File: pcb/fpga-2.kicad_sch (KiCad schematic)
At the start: 3 parts

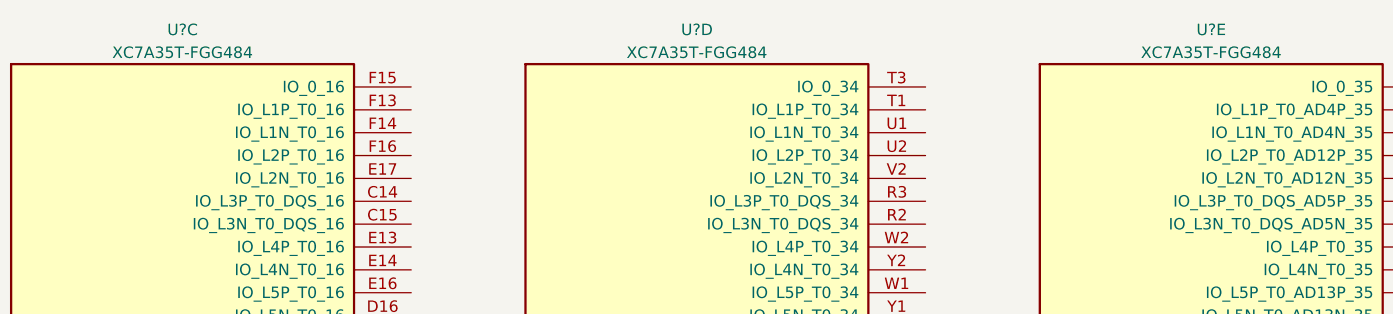
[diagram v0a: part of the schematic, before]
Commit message: addl. updates to power hierarchy
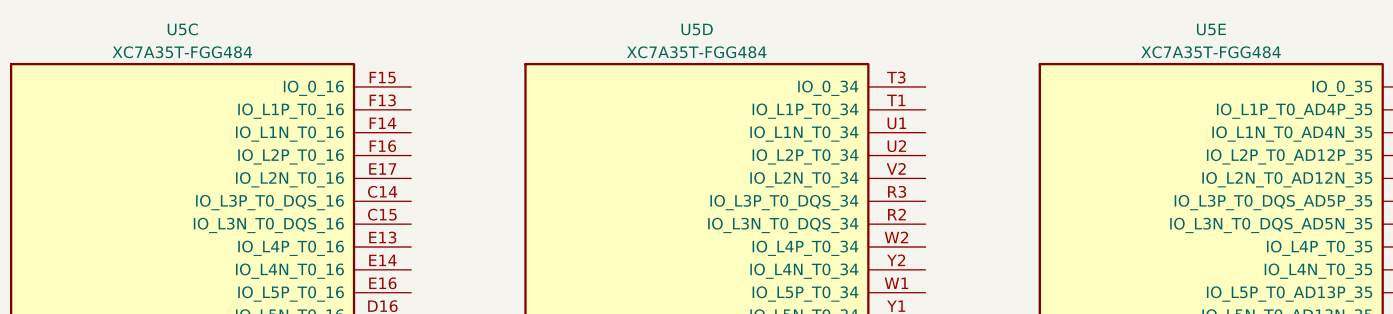
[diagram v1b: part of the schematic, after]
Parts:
- gave numbers to parts that had none: 1
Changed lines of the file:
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@@
 		(dnp no)
 		(fields_autoplaced yes)
-		(property "Reference" "U?"
+		(property "Reference" "U5"
 			(at 154.94 16.51 0)
 			(effects
@@
 			(project "RPi-HwAB-1"
 				(path "/e63e39d7-6ac0-4ffd-8aa3-1841a4541b55/6950ed9d-07bc-48b4-b7cb-d07910134e16"
-					(reference "U?")
+					(reference "U5")
 					(unit 5)
 				)
@@
 		(dnp no)
 		(fields_autoplaced yes)
-		(property "Reference" "U?"
+		(property "Reference" "U5"
 			(at 40.64 16.51 0)
 			(effects
@@
 			(project "RPi-HwAB-1"
 				(path "/e63e39d7-6ac0-4ffd-8aa3-1841a4541b55/6950ed9d-07bc-48b4-b7cb-d07910134e16"
-					(reference "U?")
+					(reference "U5")
 					(unit 3)
 				)
@@
 		(dnp no)
 		(fields_autoplaced yes)
-		(property "Reference" "U?"
+		(property "Reference" "U5"
 			(at 97.79 16.51 0)
 			(effects
@@
 			(project "RPi-HwAB-1"
 				(path "/e63e39d7-6ac0-4ffd-8aa3-1841a4541b55/6950ed9d-07bc-48b4-b7cb-d07910134e16"
-					(reference "U?")
+					(reference "U5")
 					(unit 4)
 				)

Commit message: added power sequencing through raspi gpio
additionally defined sensors
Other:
- company: (none) -> Andre S Winkel
- title: (none) -> RPi HwAB HAT+
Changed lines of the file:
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@@
 	(generator_version "9.0")
 	(paper "A4")
+	(title_block
+		(title "RPi HwAB HAT+")
+		(date "2025-08-23")
+		(rev "01")
+		(company "Andre S Winkel")
+	)
 	(symbol
 		(lib_id "FPGA_Xilinx_Artix7:XC7A35T-FGG484")

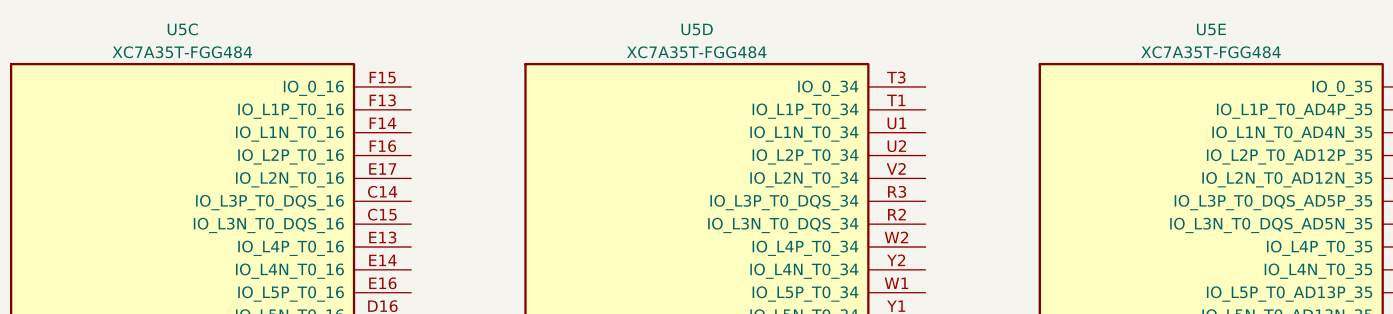
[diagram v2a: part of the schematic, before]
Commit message: reorg hierarchical, define buses
added bus definitions, aliasing, reorganized sub-sheets for hierarchical interpretation, grouped fpga. pending dram and mram addition
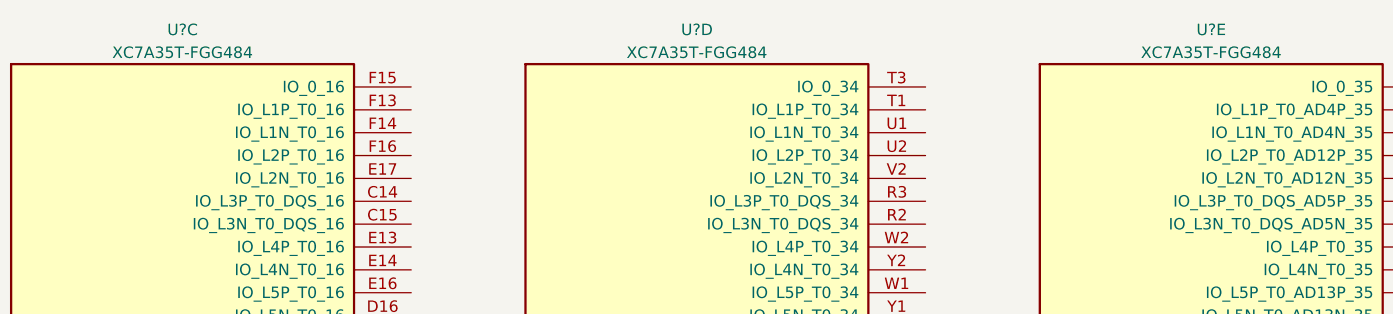
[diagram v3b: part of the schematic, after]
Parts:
- renumbered U5 to U?
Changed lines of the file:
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@@
 		(dnp no)
 		(fields_autoplaced yes)
-		(property "Reference" "U5"
+		(property "Reference" "U?"
 			(at 154.94 16.51 0)
 			(effects
@@
 		(instances
 			(project "RPi-HwAB-1"
-				(path "/e63e39d7-6ac0-4ffd-8aa3-1841a4541b55/6950ed9d-07bc-48b4-b7cb-d07910134e16"
-					(reference "U5")
+				(path "/e63e39d7-6ac0-4ffd-8aa3-1841a4541b55/59d21473-a004-4514-8090-fd93db818925/ef42fd34-c1d8-421f-b8cb-1078e483aec9"
+					(reference "U?")
 					(unit 5)
 				)
@@
 		(dnp no)
 		(fields_autoplaced yes)
-		(property "Reference" "U5"
+		(property "Reference" "U?"
 			(at 40.64 16.51 0)
 			(effects
@@
 		(instances
 			(project "RPi-HwAB-1"
-				(path "/e63e39d7-6ac0-4ffd-8aa3-1841a4541b55/6950ed9d-07bc-48b4-b7cb-d07910134e16"
-					(reference "U5")
+				(path "/e63e39d7-6ac0-4ffd-8aa3-1841a4541b55/59d21473-a004-4514-8090-fd93db818925/ef42fd34-c1d8-421f-b8cb-1078e483aec9"
+					(reference "U?")
 					(unit 3)
 				)
@@
 		(dnp no)
 		(fields_autoplaced yes)
-		(property "Reference" "U5"
+		(property "Reference" "U?"
 			(at 97.79 16.51 0)
 			(effects
@@
 		(instances
 			(project "RPi-HwAB-1"
-				(path "/e63e39d7-6ac0-4ffd-8aa3-1841a4541b55/6950ed9d-07bc-48b4-b7cb-d07910134e16"
-					(reference "U5")
+				(path "/e63e39d7-6ac0-4ffd-8aa3-1841a4541b55/59d21473-a004-4514-8090-fd93db818925/ef42fd34-c1d8-421f-b8cb-1078e483aec9"
+					(reference "U?")
 					(unit 4)
 				)

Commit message: completed bus aliasing definitions
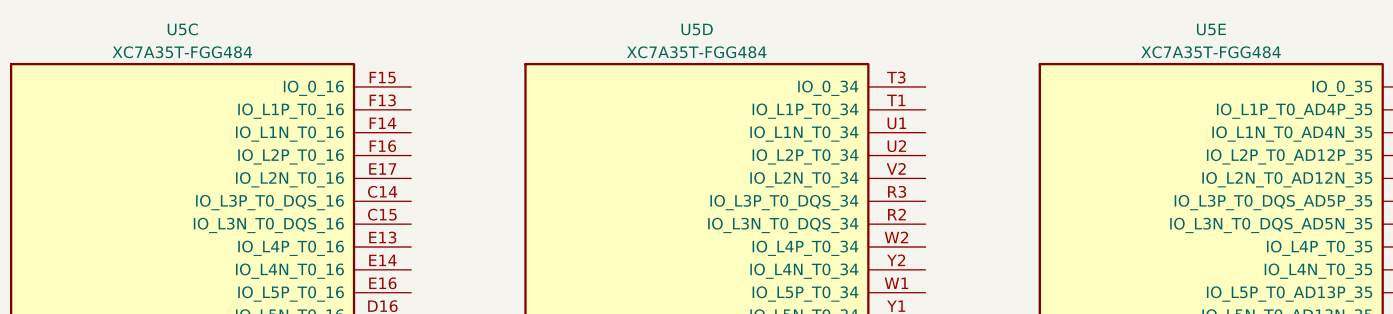
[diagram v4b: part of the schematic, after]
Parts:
- gave numbers to parts that had none: 1
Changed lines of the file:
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@@
 		(dnp no)
 		(fields_autoplaced yes)
-		(property "Reference" "U?"
+		(property "Reference" "U5"
 			(at 154.94 16.51 0)
 			(effects
@@
 			(project "RPi-HwAB-1"
 				(path "/e63e39d7-6ac0-4ffd-8aa3-1841a4541b55/59d21473-a004-4514-8090-fd93db818925/ef42fd34-c1d8-421f-b8cb-1078e483aec9"
-					(reference "U?")
+					(reference "U5")
 					(unit 5)
 				)
@@
 		(dnp no)
 		(fields_autoplaced yes)
-		(property "Reference" "U?"
+		(property "Reference" "U5"
 			(at 40.64 16.51 0)
 			(effects
@@
 			(project "RPi-HwAB-1"
 				(path "/e63e39d7-6ac0-4ffd-8aa3-1841a4541b55/59d21473-a004-4514-8090-fd93db818925/ef42fd34-c1d8-421f-b8cb-1078e483aec9"
-					(reference "U?")
+					(reference "U5")
 					(unit 3)
 				)
@@
 		(dnp no)
 		(fields_autoplaced yes)
-		(property "Reference" "U?"
+		(property "Reference" "U5"
 			(at 97.79 16.51 0)
 			(effects
@@
 			(project "RPi-HwAB-1"
 				(path "/e63e39d7-6ac0-4ffd-8aa3-1841a4541b55/59d21473-a004-4514-8090-fd93db818925/ef42fd34-c1d8-421f-b8cb-1078e483aec9"
-					(reference "U?")
+					(reference "U5")
 					(unit 4)
 				)

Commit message: saved libraries to project
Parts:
- U5: symbol FPGA_Xilinx_Artix7:XC7A35T-FGG484 -> library:XC7A35T-FGG484
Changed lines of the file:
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@@
 	)
 	(symbol
-		(lib_id "FPGA_Xilinx_Artix7:XC7A35T-FGG484")
+		(lib_id "library:XC7A35T-FGG484")
 		(at 154.94 85.09 0)
 		(unit 5)
@@
 	)
 	(symbol
-		(lib_id "FPGA_Xilinx_Artix7:XC7A35T-FGG484")
+		(lib_id "library:XC7A35T-FGG484")
 		(at 40.64 85.09 0)
 		(unit 3)
@@
 	)
 	(symbol
-		(lib_id "FPGA_Xilinx_Artix7:XC7A35T-FGG484")
+		(lib_id "library:XC7A35T-FGG484")
 		(at 97.79 85.09 0)
 		(unit 4)

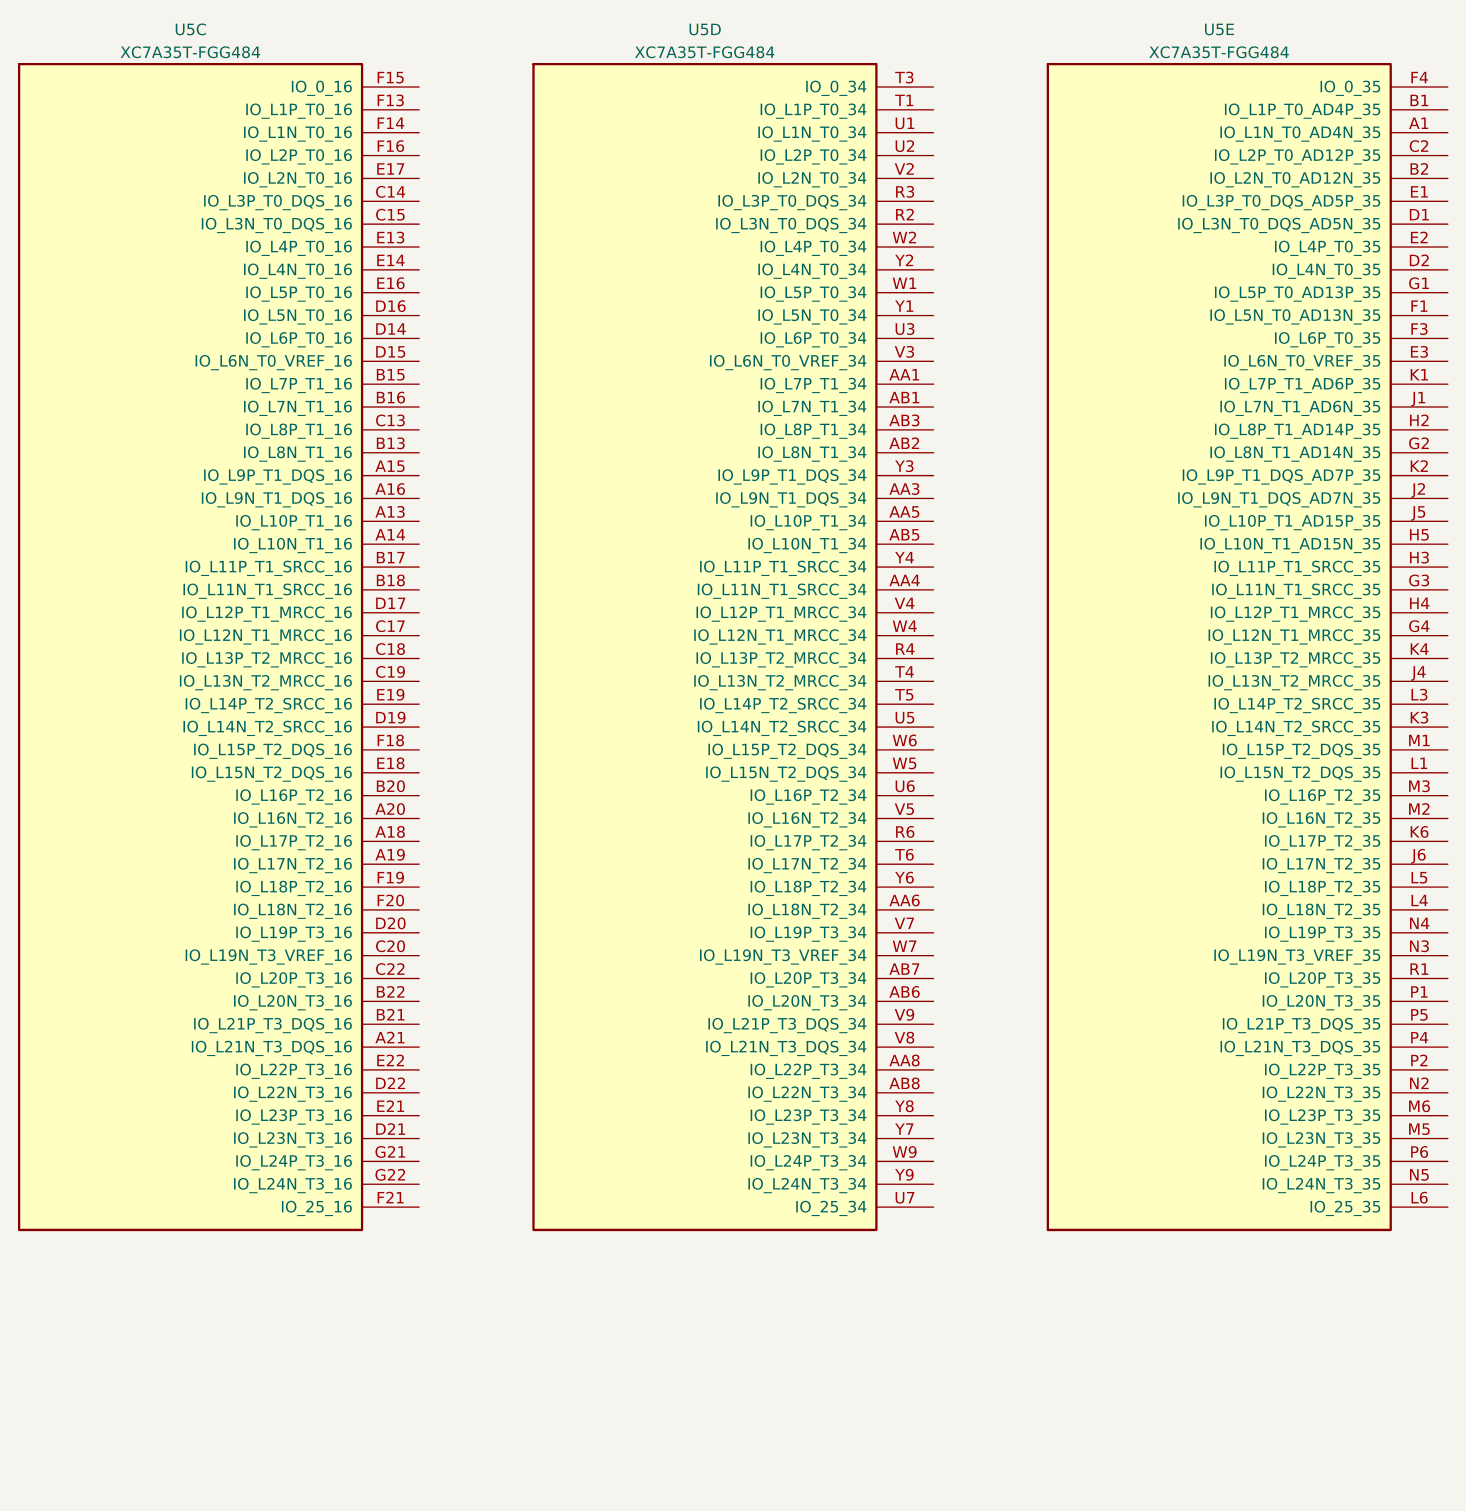
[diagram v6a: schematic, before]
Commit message: defined memory pinouts
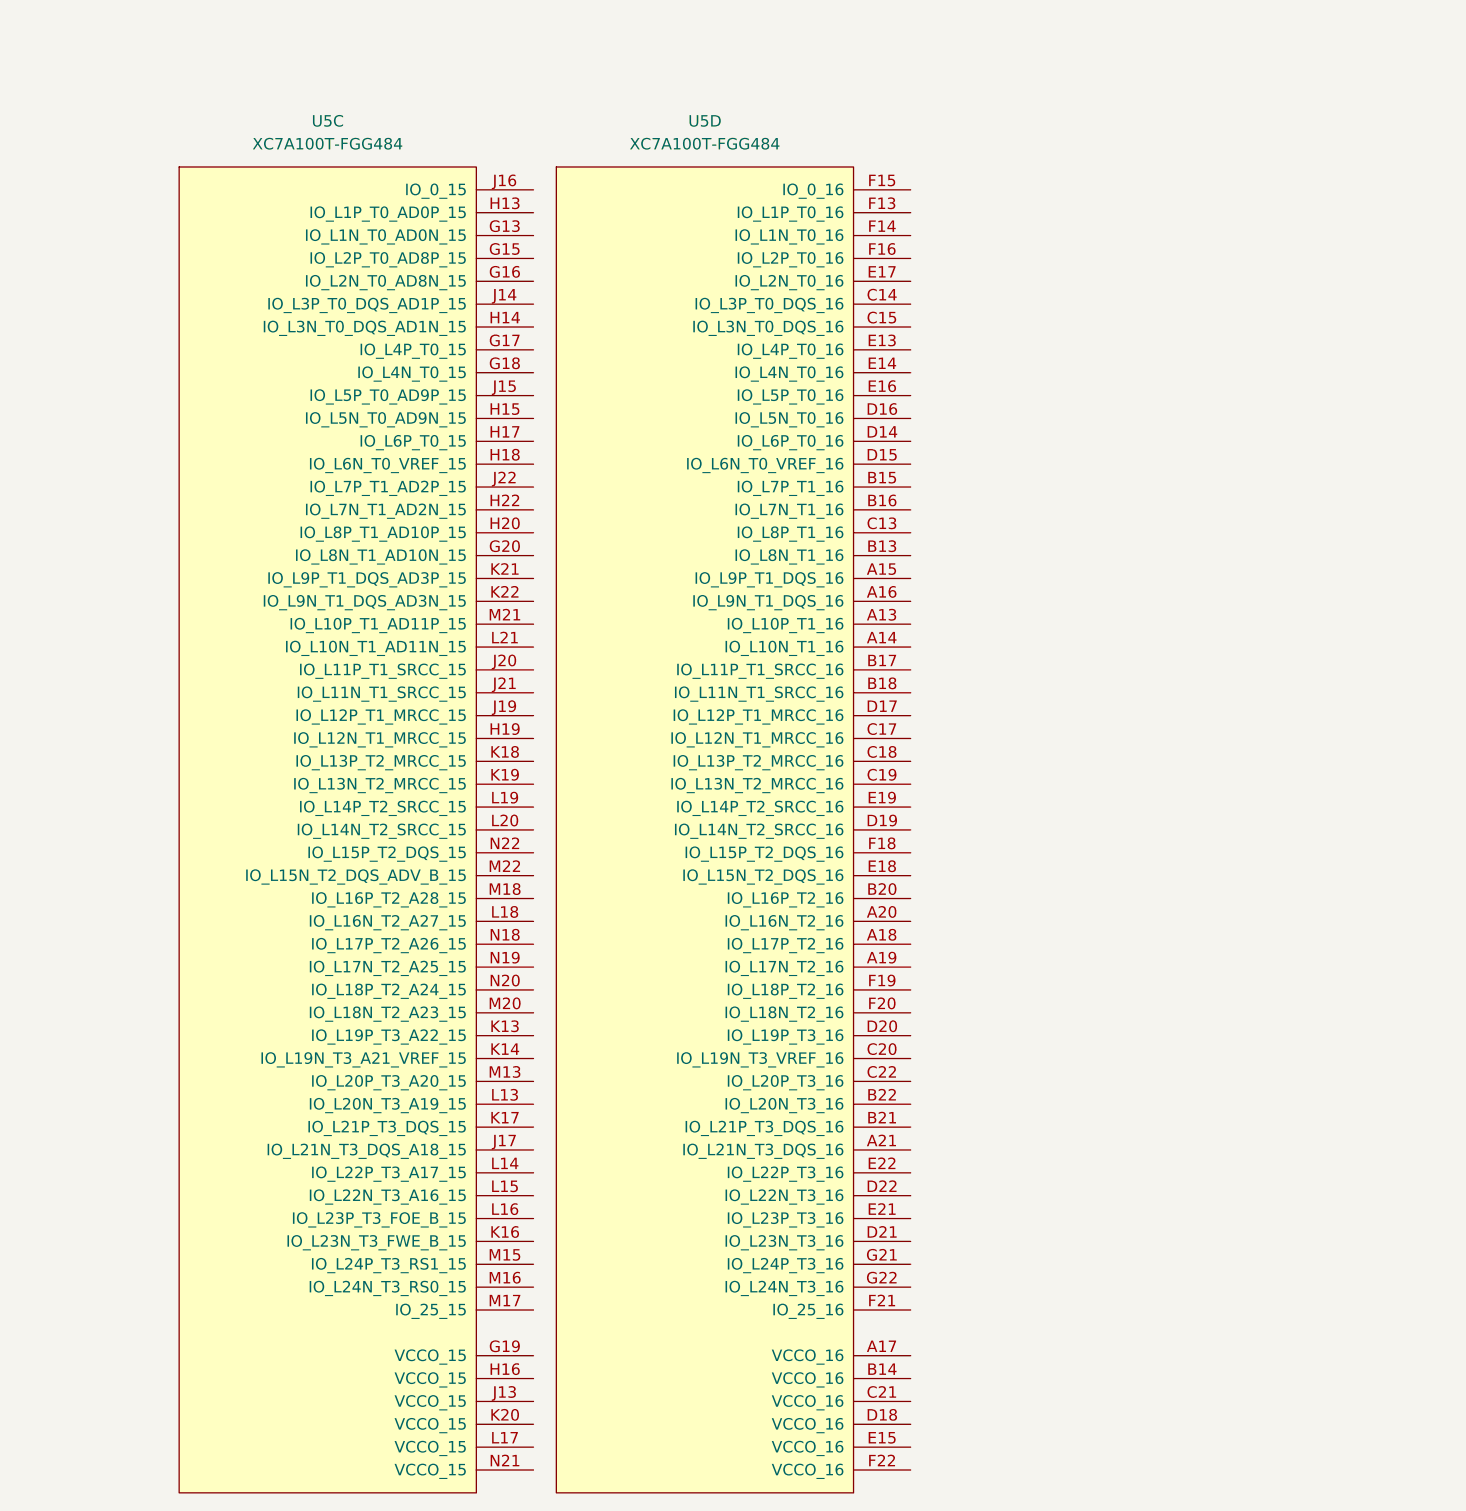
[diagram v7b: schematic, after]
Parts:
- removed U5: XC7A35T-FGG484, Package_BGA:Xilinx_FGG484, symbol library:XC7A35T-FGG484
- added U5: XC7A100T-FGG484, library:Xilinx_FGG484, symbol FPGA_Xilinx_Artix7:XC7A100T-FGG484

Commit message: power restructuring
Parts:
- U5: symbol FPGA_Xilinx_Artix7:XC7A100T-FGG484 -> library:XC7A100T-FGG484
- U5: symbol FPGA_Xilinx_Artix7:XC7A100T-FGG484 -> library:XC7A100T-FGG484_1
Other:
- moved on the sheet: U5C, U5D
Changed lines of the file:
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@@
 	)
 	(symbol
-		(lib_id "FPGA_Xilinx_Artix7:XC7A100T-FGG484")
-		(at 97.79 85.09 0)
+		(lib_id "library:XC7A100T-FGG484")
+		(at 99.06 83.82 0)
 		(unit 4)
 		(exclude_from_sim no)
@@
 		(fields_autoplaced yes)
 		(property "Reference" "U5"
-			(at 97.79 26.67 0)
+			(at 99.06 25.4 0)
 			(effects
 				(font
@@
 		)
 		(property "Value" "XC7A100T-FGG484"
-			(at 97.79 29.21 0)
+			(at 99.06 27.94 0)
 			(effects
 				(font
@@
 		)
 		(property "Footprint" "library:Xilinx_FGG484"
-			(at 97.79 85.09 0)
+			(at 99.06 83.82 0)
 			(effects
 				(font
@@
 		)
 		(property "Datasheet" ""
-			(at 97.79 85.09 0)
+			(at 99.06 83.82 0)
 			(effects
 				(font
@@
 		)
 		(property "Description" "Artix 7 T 100 XC7A100T-FGG484"
-			(at 97.79 196.85 0)
+			(at 99.06 195.58 0)
 			(effects
 				(font
@@
 		)
 		(property "Name" ""
-			(at 97.79 85.09 0)
+			(at 99.06 83.82 0)
 			(effects
 				(font
@@
 	)
 	(symbol
-		(lib_id "FPGA_Xilinx_Artix7:XC7A100T-FGG484")
-		(at 55.88 85.09 0)
+		(lib_name "XC7A100T-FGG484_1")
+		(lib_id "library:XC7A100T-FGG484_1")
+		(at 53.34 83.82 0)
 		(unit 3)
 		(exclude_from_sim no)
@@
 		(fields_autoplaced yes)
 		(property "Reference" "U5"
-			(at 55.88 26.67 0)
+			(at 53.34 25.4 0)
 			(effects
 				(font
@@
 		)
 		(property "Value" "XC7A100T-FGG484"
-			(at 55.88 29.21 0)
+			(at 53.34 27.94 0)
 			(effects
 				(font
@@
 		)
 		(property "Footprint" "library:Xilinx_FGG484"
-			(at 55.88 85.09 0)
+			(at 53.34 83.82 0)
 			(effects
 				(font
@@
 		)
 		(property "Datasheet" ""
-			(at 55.88 85.09 0)
+			(at 53.34 83.82 0)
 			(effects
 				(font
@@
 		)
 		(property "Description" "Artix 7 T 100 XC7A100T-FGG484"
-			(at 55.88 196.85 0)
+			(at 53.34 195.58 0)
 			(effects
 				(font
@@
 		)
 		(property "Name" ""
-			(at 55.88 85.09 0)
-			(effects
-				(font
+			(at 53.34 83.82 0)
+			(effects
+				(font
